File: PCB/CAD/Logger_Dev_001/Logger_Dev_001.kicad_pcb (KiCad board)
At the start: 2 copper layers, 54.5 x 67 mm, 74 parts, among them J1 Conn_Coaxial, J3 Micro_SD_Card_Det1, J4 Connector, USB-TYPE-C-16P, Q1 BC847BS, Q2 MMBT3904, U1 L76-M33, U2 ESP32-C6-WROOM-1, U5 AMS1117, U6 CP2102-GMR

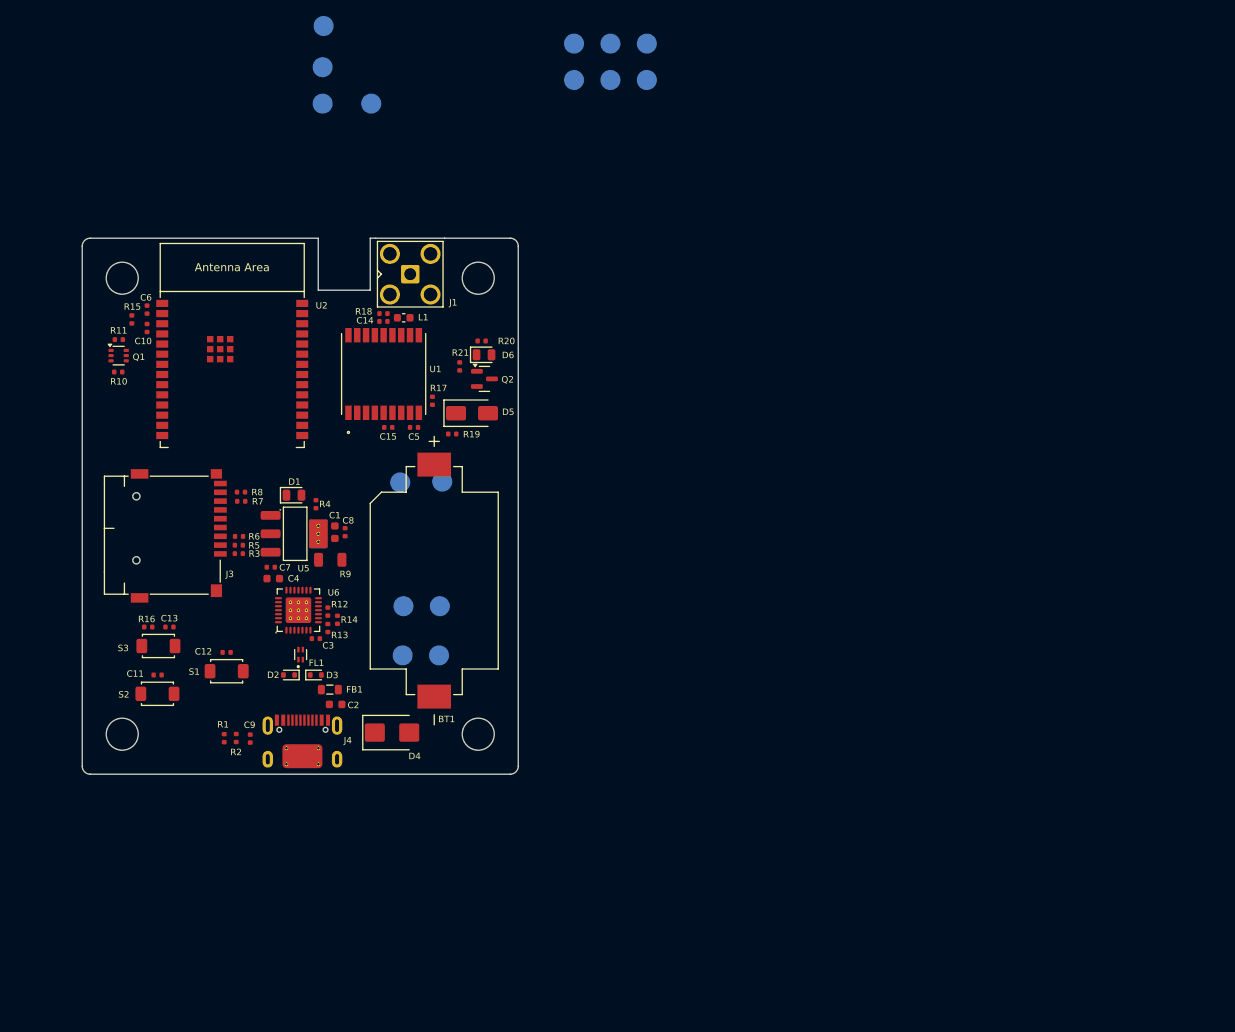
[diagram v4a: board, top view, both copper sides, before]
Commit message: PCB Board Needing Traces
Slight rearrangement of components.
To route power rails mostly around the outside
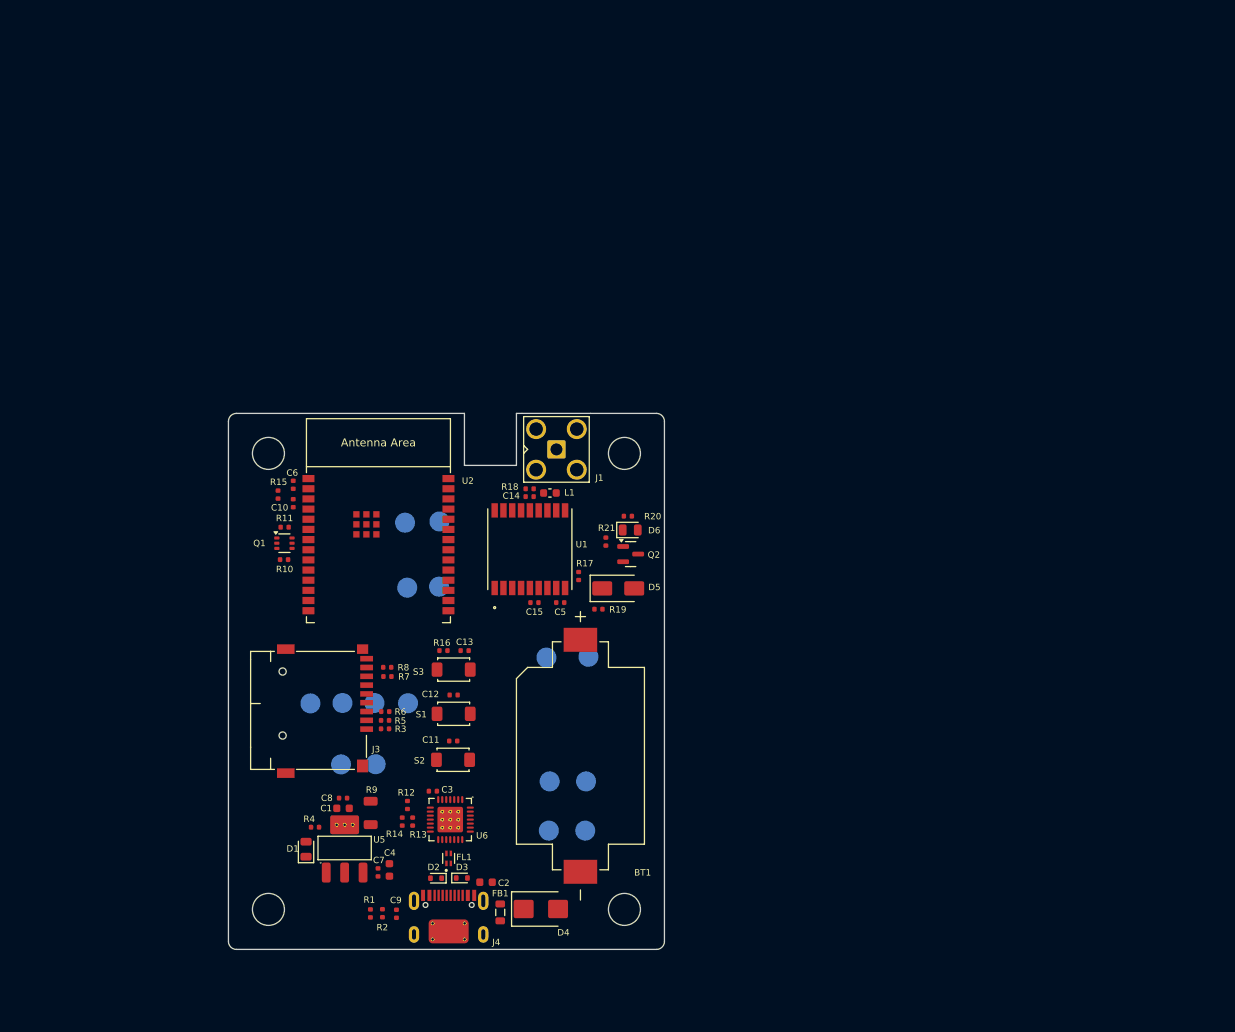
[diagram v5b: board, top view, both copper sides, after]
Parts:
- moved TP9 96.2 mm to (132.8, 115.8)
- moved TP10 90.4 mm to (137.2, 115.8)
- moved TP7 89.2 mm to (137.0, 108.1)
- moved TP11 88.8 mm to (129.0, 108.2)
- moved TP8 83.4 mm to (141.2, 108.1)
- moved TP12 83.1 mm to (133.0, 108.1)
- moved TP1 66.5 mm to (145.1, 93.6)
- moved TP15 63.6 mm to (145.2, 85.4)
- moved TP2 61.4 mm to (141.1, 93.7)
- moved TP16 52.6 mm to (140.8, 85.6)
- moved D1 44.3 mm to (128.5, 126.4), turned to 90 degrees
- moved C7 40.4 mm to (137.5, 129.3), turned to 90 degrees
- moved R4 40.4 mm to (129.6, 123.6), turned to 180 degrees
- moved U5 39.9 mm to (133.3, 126.3), turned to -90 degrees
- moved C4 39.2 mm to (138.9, 129.0), turned to 90 degrees
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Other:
- board text added: "DTR, RTS"
- board text added: "Extra Btn, GND"
- board text added: "SDIO CMD, CLK"

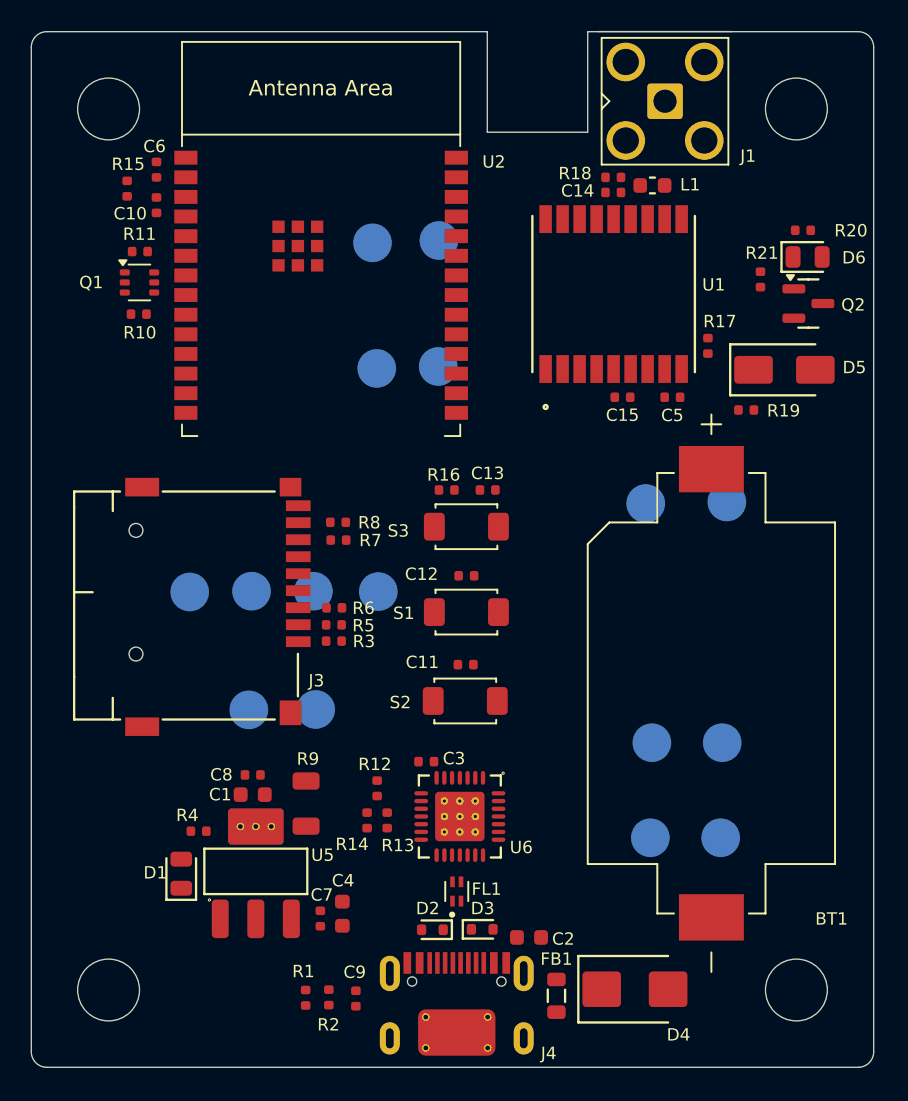
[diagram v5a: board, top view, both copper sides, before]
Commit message: Logger_Dev_001 Board Update
Constraints for DRC updated

Still to:
-assign Net classes and trace sizing
-wire traces with DCR
-check BOM
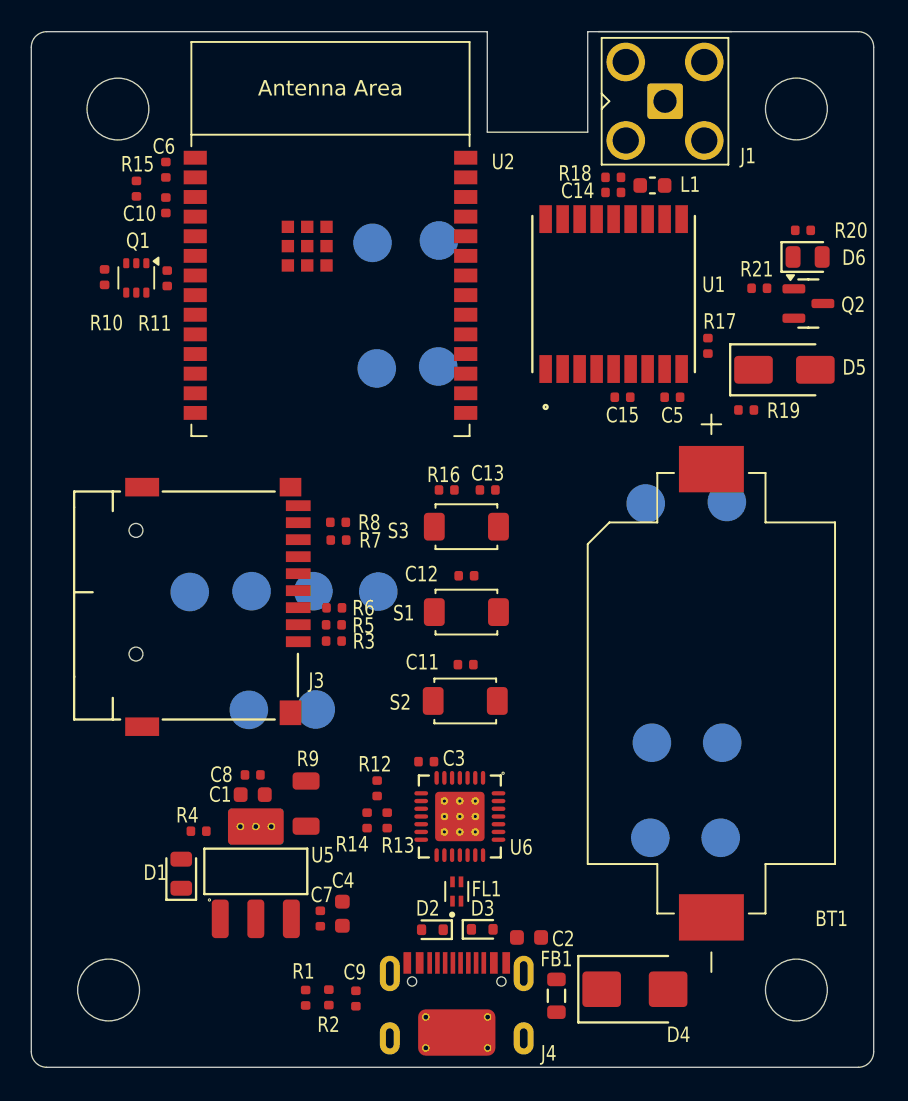
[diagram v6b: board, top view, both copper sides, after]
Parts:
- moved R10 3.26 mm to (123.5, 87.8), turned to 90 degrees
- moved R11 2.47 mm to (127.6, 87.9), turned to -90 degrees
- moved R15 0.61 mm to (125.6, 82.1)
- moved C10 0.61 mm to (127.5, 83.1)
- moved C6 0.61 mm to (127.5, 80.8)
- moved U2 0.61 mm to (138.1, 88.3)
- moved R21 0.58 mm to (165.9, 88.5), turned to 0 degrees
- moved Q1 0.36 mm to (125.6, 87.8), turned to -90 degrees
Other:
- outline, holes or cut-outs redrawn

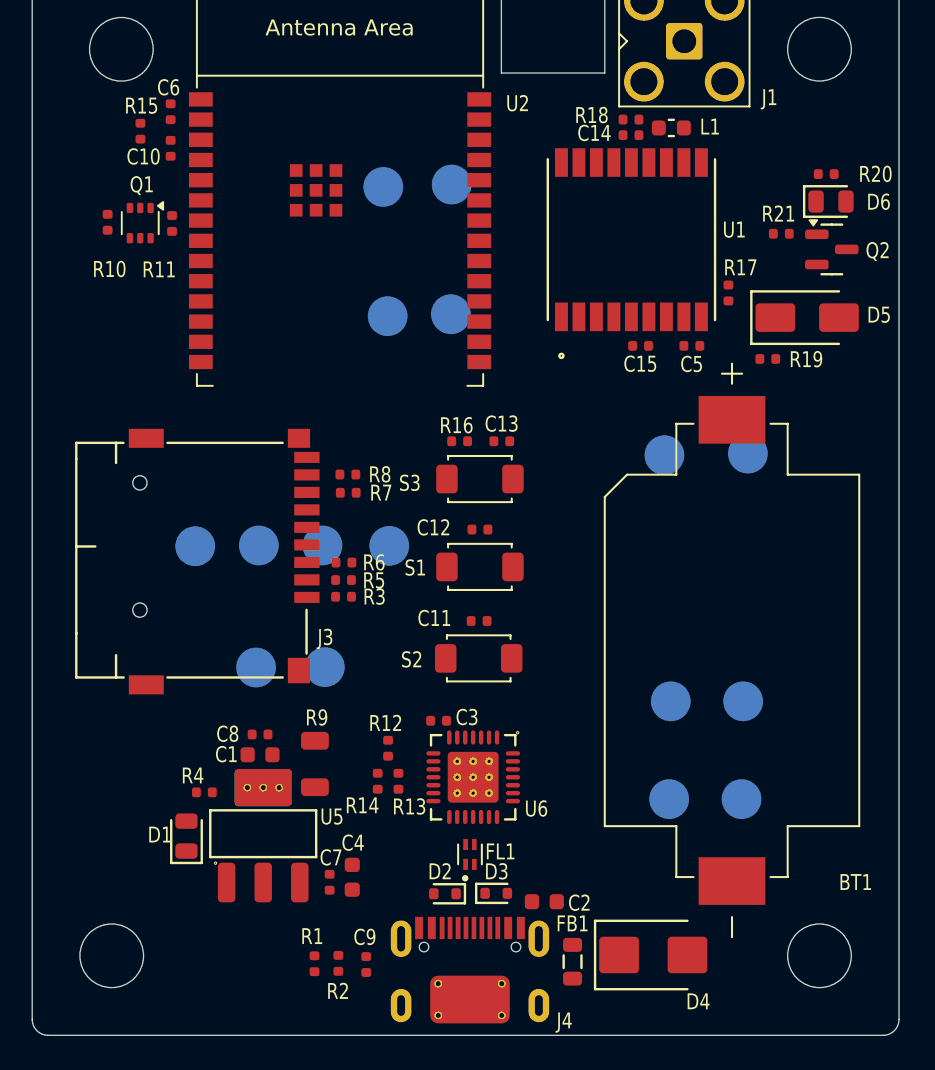
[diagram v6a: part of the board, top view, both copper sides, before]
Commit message: PCB Board Initial Trace
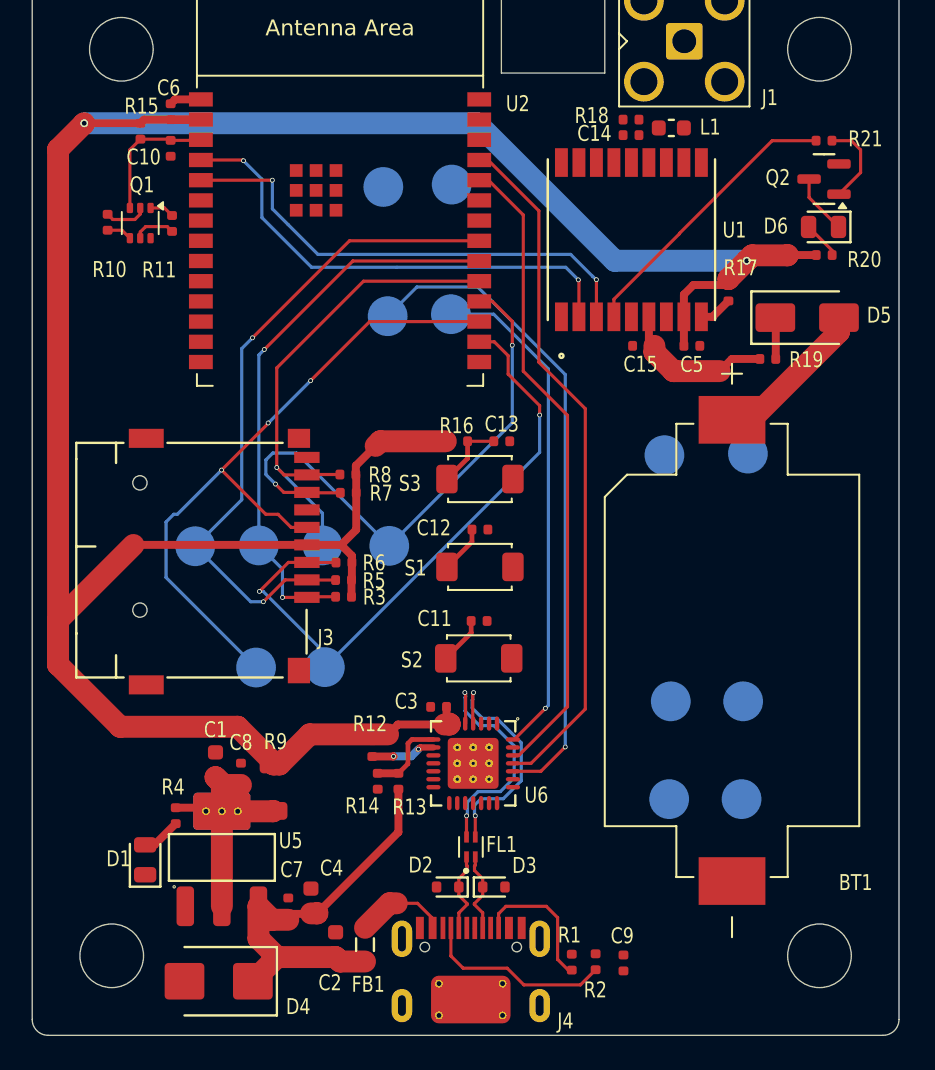
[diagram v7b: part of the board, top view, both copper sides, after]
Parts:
- moved D4 27.4 mm to (130.5, 135.5), turned to 180 degrees
- moved C9 16.2 mm to (155.9, 134.3)
- moved R1 16.2 mm to (152.7, 134.3)
- moved R2 16.2 mm to (154.2, 134.3)
- moved C2 13.4 mm to (137.8, 133.2), turned to 90 degrees
- moved FB1 13.1 mm to (139.7, 133.2), turned to 90 degrees
- moved R21 6.44 mm to (168.6, 82.7)
- moved R20 5.09 mm to (168.6, 89.8)
- moved Q2 4.45 mm to (168.6, 85.1), turned to 180 degrees
- moved R9 3.00 mm to (133.9, 123.3)
- moved U5 3.00 mm to (130.7, 127.8)
- moved C4 3.00 mm to (136.3, 130.5)
- moved D1 3.00 mm to (125.9, 127.9)
- moved C7 3.00 mm to (134.9, 130.8)
- moved C1 2.87 mm to (130.3, 121.9), turned to 90 degrees
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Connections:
- D2 pad 1: Net-(D2-Pad1) -> /USB C COMs 3v3 Power Input Module/USB_UNF_D-
- D3 pad 1: Net-(D3-Pad1) -> /USB C COMs 3v3 Power Input Module/USB_UNF_D+
- FL1 pad 1: Net-(D2-Pad1) -> /USB C COMs 3v3 Power Input Module/USB_UNF_D-
- FL1 pad 2: /USB C COMs 3v3 Power Input Module/D-_USB -> /USB C COMs 3v3 Power Input Module/USB_D-
- FL1 pad 3: /USB C COMs 3v3 Power Input Module/D+_USB -> /USB C COMs 3v3 Power Input Module/USB_D+
- FL1 pad 4: Net-(D3-Pad1) -> /USB C COMs 3v3 Power Input Module/USB_UNF_D+
- J4 pad A6: Net-(D3-Pad1) -> /USB C COMs 3v3 Power Input Module/USB_UNF_D+
- J4 pad A7: Net-(D2-Pad1) -> /USB C COMs 3v3 Power Input Module/USB_UNF_D-
- J4 pad B6: Net-(D3-Pad1) -> /USB C COMs 3v3 Power Input Module/USB_UNF_D+
- J4 pad B7: Net-(D2-Pad1) -> /USB C COMs 3v3 Power Input Module/USB_UNF_D-
- TP5 pad 1: /USB C COMs 3v3 Power Input Module/D+_USB -> /USB C COMs 3v3 Power Input Module/USB_UNF_D+
- TP6 pad 1: /USB C COMs 3v3 Power Input Module/D-_USB -> /USB C COMs 3v3 Power Input Module/USB_UNF_D-
- U6 pad 4: /USB C COMs 3v3 Power Input Module/D+_USB -> /USB C COMs 3v3 Power Input Module/USB_D+
- U6 pad 5: /USB C COMs 3v3 Power Input Module/D-_USB -> /USB C COMs 3v3 Power Input Module/USB_D-
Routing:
- net 3v3_VCC: track 0.00 -> 169.5 mm, vias 0 -> 2
- net /USBC_RX: track 0.00 -> 43.6 mm
- net /SDIO_CLK: track 0.00 -> 43.3 mm, vias 0 -> 3
- net /USB C COMs 3v3 Power Input Module/RTS: track 0.00 -> 43.2 mm, vias 0 -> 1
- net /SDIO_DATA3: track 0.00 -> 42.2 mm, vias 0 -> 2
- net /USBC_TX: track 0.00 -> 40.4 mm
- net /SDIO_CMD: track 0.00 -> 40.4 mm, vias 0 -> 2
- net /SDIO_DATA0: track 0.00 -> 36.3 mm, vias 0 -> 2
- net /SDIO_DATA2: track 0.00 -> 35.5 mm, vias 0 -> 2
- net /USB C COMs 3v3 Power Input Module/DTR: track 0.00 -> 33.4 mm, vias 0 -> 1
- net /SDIO_DATA1: track 0.00 -> 31.5 mm, vias 0 -> 1
- net /GPS_RX: track 0.00 -> 30.9 mm, vias 0 -> 2
- net /GPS_TX: track 0.00 -> 30.6 mm, vias 0 -> 2
- net VUSB: track 0.00 -> 25.5 mm
- net /GPS Module/1PPS: track 0.00 -> 18.0 mm
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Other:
- board text removed: "USB D+, D-"

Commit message: PCB Trace Update
Still to add ground plane and check via sizing
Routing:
- net /EN: track 11.5 -> 62.9 mm, vias 0 -> 2
- net /BTN_FUNCTION: track 4.56 -> 50.3 mm, vias 0 -> 1
- net /GPIO9_BOOT: track 3.00 -> 43.4 mm, vias 0 -> 2
- net /USB C COMs 3v3 Power Input Module/RTS: track 43.2 -> 68.8 mm, vias 1 -> 2
- net /USB C COMs 3v3 Power Input Module/DTR: track 33.4 -> 57.8 mm, vias 1 -> 2
- net /GPS_TX: track 30.6 -> 53.0 mm
- net /USBC_TX: track 40.4 -> 53.3 mm, vias 0 -> 1
- net /GPS_RX: track 30.9 -> 43.7 mm
- net /SDIO_DATA0: track 36.3 -> 28.9 mm
- net RF_GND: track 0.00 -> 7.13 mm
- net /USBC_RX: track 43.6 -> 49.7 mm, vias 0 -> 1
- net /SDIO_CLK: track 43.3 -> 46.1 mm, vias 3 -> 2
- net /SDIO_DATA1: vias 1 -> 2
